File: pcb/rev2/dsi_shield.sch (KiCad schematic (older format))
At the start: 18 parts, among them CN10 CVBS In, CN5 IOH, CN6 POWER_UNO, CN7 IOL, CN8 AD, IC12 OSC_25MHZ_PERICOM_FNETHE025

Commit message: pcb wip
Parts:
- B1, B2, B3, B4: footprint c350h200 -> Pads:c350h200
- C17: footprint CAPC1608X90N -> Capacitors SMD:CAPC1608X90N
- D9: footprint SOD3715X145N -> ICs And Semiconductors SMD:SOD3715X145N
- FTG1, FTG2, FTG3, FTG4, FTG5, FTG6: footprint FIDUCIAL_TOP_S100-200 -> Pads:FIDUCIAL_TOP_S100-200
- IC12: footprint OSC_PERICOM_FNETHE025 -> ICs And Semiconductors SMD:OSC_PERICOM_FNETHE025
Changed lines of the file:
@@
 F 0 "IC12" H 6150 7415 50  0000 C CNN
 F 1 "OSC_25MHZ_PERICOM_FNETHE025" H 5850 6660 60  0001 L CNN
-F 2 "OSC_PERICOM_FNETHE025" H 5850 5760 60  0001 L CNN
+F 2 "ICs And Semiconductors SMD:OSC_PERICOM_FNETHE025" H 5850 5760 60  0001 L CNN
 F 3 "\\cern.ch\\dfs\\Applications\\Altium\\Datasheets\\OSC_PERICOM_FNETHE025.pdf" H 5850 6480 60  0001 L CNN
 F 4 "25MHz" H 6150 7324 50  0000 C CNN "~"
@@
 F 0 "C17" V 5754 7860 50  0000 L CNN
 F 1 "CC0603_100NF_100V_10%_X7R" H 5650 7490 60  0001 L CNN
-F 2 "CAPC1608X90N" H 5650 6680 60  0001 L CNN
+F 2 "Capacitors SMD:CAPC1608X90N" H 5650 6680 60  0001 L CNN
 F 3 "\\cern.ch\\dfs\\Applications\\Altium\\Datasheets\\CC0603_MURATA_GRM188R72A104KA35D.pdf" H 5650 7310 60  0001 L CNN
 F 4 "100nF" V 5845 7860 50  0000 L CNN "~"
@@
 F 0 "B1" H 6600 9950 50  0000 C CNN
 F 1 "PLATED_HOLE2.0_PAD3.5" H 6500 9780 60  0001 L CNN
-F 2 "c350h200" H 6500 8970 60  0001 L CNN
+F 2 "Pads:c350h200" H 6500 8970 60  0001 L CNN
 F 3 "Undefined" H 6500 9600 60  0001 L CNN
 F 4 "Plated Hole" H 6500 9510 60  0001 L CNN "Field4"
@@
 F 0 "B2" H 6600 10050 50  0000 C CNN
 F 1 "PLATED_HOLE2.0_PAD3.5" H 6500 9880 60  0001 L CNN
-F 2 "c350h200" H 6500 9070 60  0001 L CNN
+F 2 "Pads:c350h200" H 6500 9070 60  0001 L CNN
 F 3 "Undefined" H 6500 9700 60  0001 L CNN
 F 4 "Plated Hole" H 6500 9610 60  0001 L CNN "Field4"
@@
 F 0 "B3" H 6600 10150 50  0000 C CNN
 F 1 "PLATED_HOLE2.0_PAD3.5" H 6500 9980 60  0001 L CNN
-F 2 "c350h200" H 6500 9170 60  0001 L CNN
+F 2 "Pads:c350h200" H 6500 9170 60  0001 L CNN
 F 3 "Undefined" H 6500 9800 60  0001 L CNN
 F 4 "Plated Hole" H 6500 9710 60  0001 L CNN "Field4"
@@
 F 0 "B4" H 6600 10250 50  0000 C CNN
 F 1 "PLATED_HOLE2.0_PAD3.5" H 6500 10080 60  0001 L CNN
-F 2 "c350h200" H 6500 9270 60  0001 L CNN
+F 2 "Pads:c350h200" H 6500 9270 60  0001 L CNN
 F 3 "Undefined" H 6500 9900 60  0001 L CNN
 F 4 "Plated Hole" H 6500 9810 60  0001 L CNN "Field4"
@@
 F 0 "FTG1" H 7038 10050 50  0000 L CNN
 F 1 "FIDUCIAL_TARGET_S100-200" H 6950 9900 60  0001 L CNN
-F 2 "FIDUCIAL_TOP_S100-200" H 6950 9090 60  0001 L CNN
+F 2 "Pads:FIDUCIAL_TOP_S100-200" H 6950 9090 60  0001 L CNN
 F 3 "Undefined" H 6950 9720 60  0001 L CNN
 F 4 "~~" H 6950 9630 60  0001 L CNN "Field4"
@@
 F 0 "FTG2" H 7438 10050 50  0000 L CNN
 F 1 "FIDUCIAL_TARGET_S100-200" H 7350 9900 60  0001 L CNN
-F 2 "FIDUCIAL_TOP_S100-200" H 7350 9090 60  0001 L CNN
+F 2 "Pads:FIDUCIAL_TOP_S100-200" H 7350 9090 60  0001 L CNN
 F 3 "Undefined" H 7350 9720 60  0001 L CNN
 F 4 "~~" H 7350 9630 60  0001 L CNN "Field4"
@@
 F 0 "FTG6" H 7438 10350 50  0000 L CNN
 F 1 "FIDUCIAL_TARGET_S100-200" H 7350 10200 60  0001 L CNN
-F 2 "FIDUCIAL_TOP_S100-200" H 7350 9390 60  0001 L CNN
+F 2 "Pads:FIDUCIAL_TOP_S100-200" H 7350 9390 60  0001 L CNN
 F 3 "Undefined" H 7350 10020 60  0001 L CNN
 F 4 "~~" H 7350 9930 60  0001 L CNN "Field4"
@@
 F 0 "FTG5" H 7038 10350 50  0000 L CNN
 F 1 "FIDUCIAL_TARGET_S100-200" H 6950 10200 60  0001 L CNN
-F 2 "FIDUCIAL_TOP_S100-200" H 6950 9390 60  0001 L CNN
+F 2 "Pads:FIDUCIAL_TOP_S100-200" H 6950 9390 60  0001 L CNN
 F 3 "Undefined" H 6950 10020 60  0001 L CNN
 F 4 "~~" H 6950 9930 60  0001 L CNN "Field4"
@@
 F 0 "FTG4" H 7838 10350 50  0000 L CNN
 F 1 "FIDUCIAL_TARGET_S100-200" H 7750 10200 60  0001 L CNN
-F 2 "FIDUCIAL_TOP_S100-200" H 7750 9390 60  0001 L CNN
+F 2 "Pads:FIDUCIAL_TOP_S100-200" H 7750 9390 60  0001 L CNN
 F 3 "Undefined" H 7750 10020 60  0001 L CNN
 F 4 "~~" H 7750 9930 60  0001 L CNN "Field4"
@@
 F 0 "FTG3" H 7838 10050 50  0000 L CNN
 F 1 "FIDUCIAL_TARGET_S100-200" H 7750 9900 60  0001 L CNN
-F 2 "FIDUCIAL_TOP_S100-200" H 7750 9090 60  0001 L CNN
+F 2 "Pads:FIDUCIAL_TOP_S100-200" H 7750 9090 60  0001 L CNN
 F 3 "Undefined" H 7750 9720 60  0001 L CNN
 F 4 "~~" H 7750 9630 60  0001 L CNN "Field4"
@@
 F 0 "D9" V 1496 4060 50  0000 R CNN
 F 1 "MBR0530PbF" V 1405 4060 50  0000 R CNN
-F 2 "SOD3715X145N" H 1300 3010 60  0001 L CNN
+F 2 "ICs And Semiconductors SMD:SOD3715X145N" H 1300 3010 60  0001 L CNN
 F 3 "\\cern.ch\\dfs\\Applications\\Altium\\Datasheets\\MBR0530PBF.pdf" H 1300 3730 60  0001 L CNN
 F 4 "MBR0530PbF" H 1300 3640 60  0001 L CNN "Part Number"

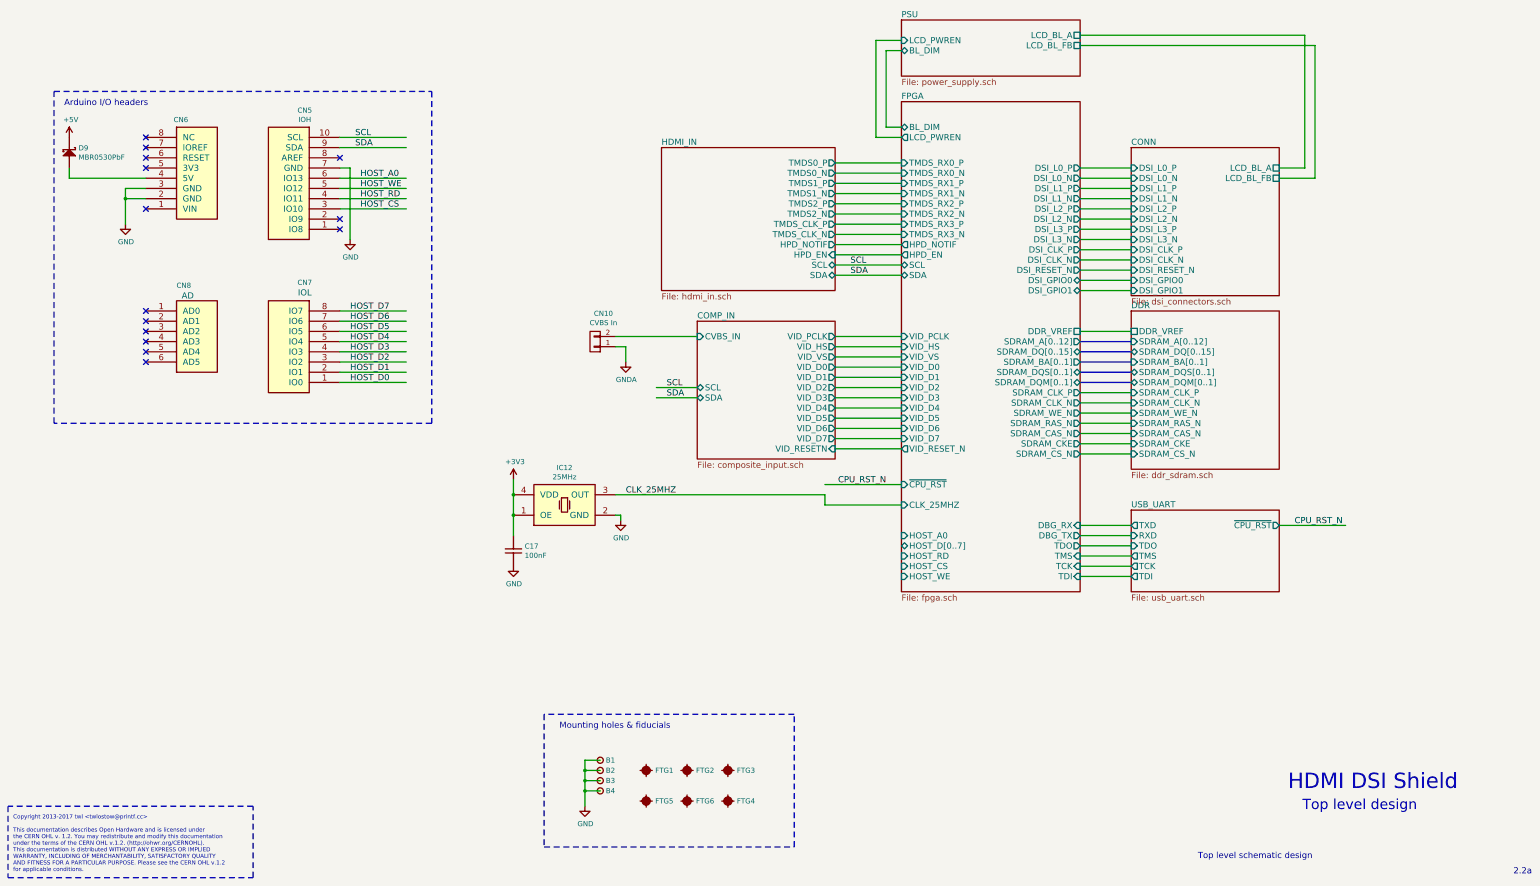
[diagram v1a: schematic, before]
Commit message: Completed port to KiCad, passes DRC+LVS. NOT MANUFACTURED.
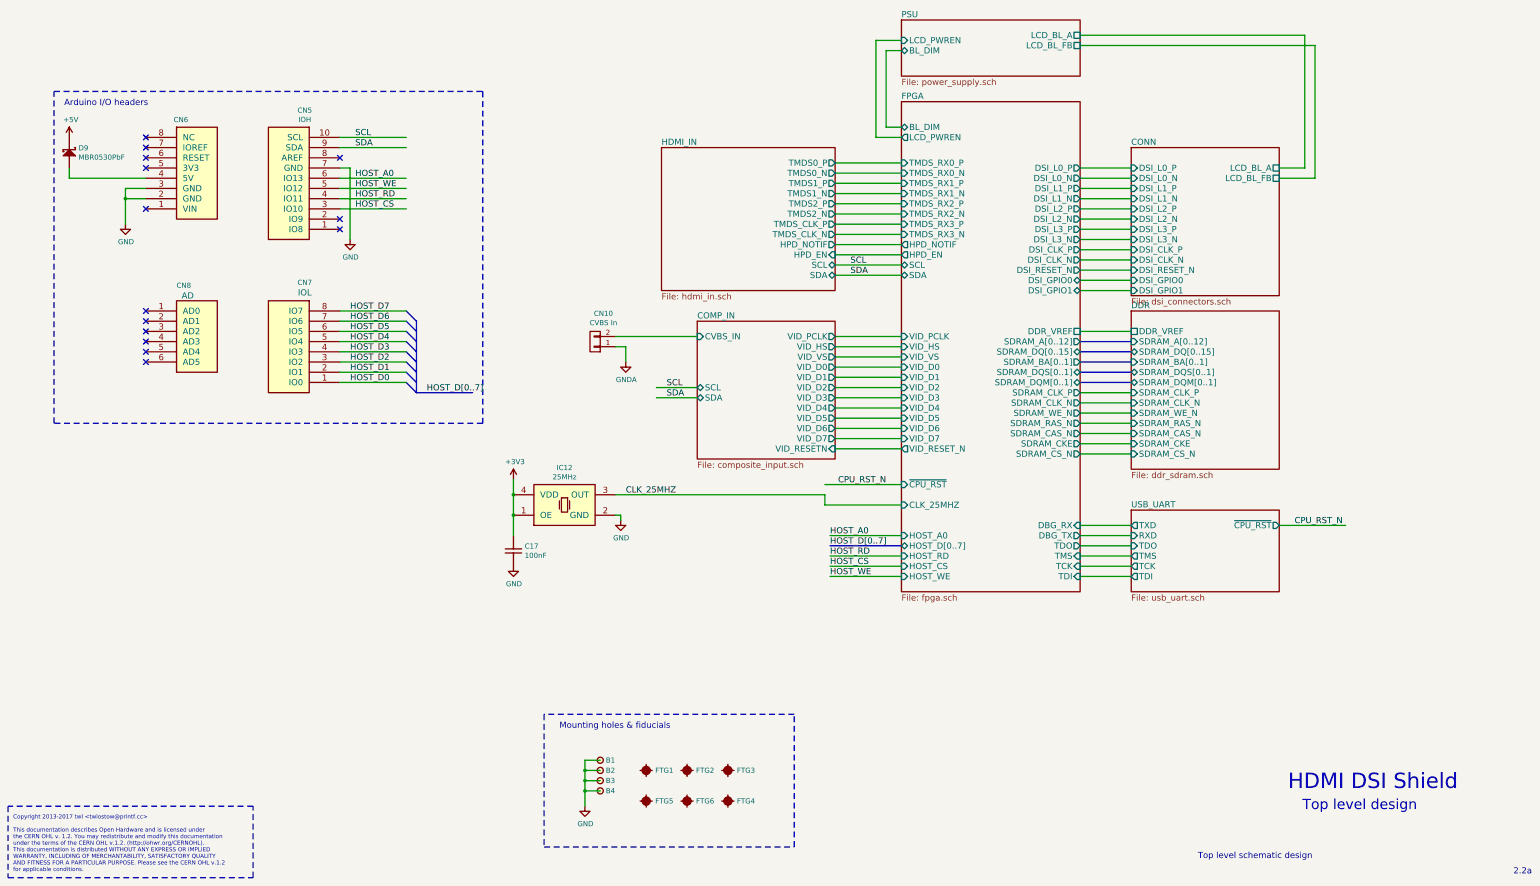
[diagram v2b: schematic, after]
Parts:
- CN10: footprint (none) -> Pin_Headers:Pin_Header_Straight_1x02; Fieldname (none) -> Value
- CN5: footprint (none) -> Pin_Headers:Pin_Header_Straight_1x10; Fieldname (none) -> Value
- CN6: footprint (none) -> Pin_Headers:Pin_Header_Straight_1x08; Fieldname (none) -> Value
- CN7: footprint (none) -> Pin_Headers:Pin_Header_Straight_1x08
- CN8: footprint (none) -> Pin_Headers:Pin_Header_Straight_1x06
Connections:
- net labels added: HOST_D[0..7]
- wire segments 102 -> 106

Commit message: axi4/zynq version: wip
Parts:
- B1, B2, B3, B4: symbol PLATED_HOLE2.0_PAD3.5 -> dsi_shield-rescue:PLATED_HOLE2.0_PAD3.5-
- C17: symbol CC0603_100NF_100V_10%_X7R -> dsi_shield-rescue:CC0603_100NF_100V_10%_X7R-
- CN10: symbol CONN_01X02 -> dsi_shield-rescue:CONN_01X02-
- CN5: symbol IOH -> dsi_shield-rescue:IOH-
- CN6: symbol POWER_UNO -> dsi_shield-rescue:POWER_UNO-
- CN7: symbol IOL -> dsi_shield-rescue:IOL-
- CN8: symbol AD -> dsi_shield-rescue:AD-
- D9: symbol MBR0530PbF -> dsi_shield-rescue:MBR0530PbF-
- FTG1, FTG2, FTG3, FTG4, FTG5, FTG6: symbol FIDUCIAL_TARGET_S100-200 -> dsi_shield-rescue:FIDUCIAL_TARGET_S100-200-
- IC12: symbol OSC_25MHZ_PERICOM_FNETHE025 -> dsi_shield-rescue:OSC_25MHZ_PERICOM_FNETHE025-
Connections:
- wire segments 106 -> 112
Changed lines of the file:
@@
-EESchema Schematic File Version 2
-LIBS:Capacitors Networks THD
-LIBS:Capacitors Networks SMD
-LIBS:Capacitors THD
-LIBS:Capacitors SMD
-LIBS:Miscellaneous
-LIBS:HARWIN
-LIBS:LEMO
-LIBS:WEIDMULLER
-LIBS:FCI
-LIBS:MOLEX
-LIBS:TYCO
-LIBS:ERNI
-LIBS:MENTOR
-LIBS:SAMTEC
-LIBS:STELVIO-KONTEK COMATEL
-LIBS:AMPHENOL
-LIBS:HARTING
-LIBS:3M
-LIBS:Pads
-LIBS:Switches
-LIBS:Relays
-LIBS:Heat-Sinks
-LIBS:Fasteners & Fixings
-LIBS:Batteries
-LIBS:Fuses
-LIBS:Metal Screening Box
-LIBS:Sockets
-LIBS:Regulators
-LIBS:Transistors
-LIBS:Power Supplies
-LIBS:Analog & Interface
-LIBS:Sensors
-LIBS:Logic
-LIBS:Optocouplers
-LIBS:Standard Logic
-LIBS:DC-DC Converters
-LIBS:Operational Amplifiers
-LIBS:Crystals & Oscillators
-LIBS:Diodes
-LIBS:LEDs & Displays
-LIBS:PCB Modules
-LIBS:Bonding
-LIBS:Resistors THD
-LIBS:Potentiometers SMD
-LIBS:Thermistors And Varistors
-LIBS:Potentiometers THD
-LIBS:Resistor Networks THD
-LIBS:Resistors SMD
-LIBS:Resistor Networks SMD
-LIBS:Transformers
-LIBS:Inductors SMD
-LIBS:Inductors THD
-LIBS:Cores
-LIBS:power
-LIBS:conn
-LIBS:dsi_shield
+EESchema Schematic File Version 4
 LIBS:dsi_shield-cache
 EELAYER 26 0
@@
 $EndSheet
 $Comp
-L OSC_25MHZ_PERICOM_FNETHE025 IC12
+L dsi_shield-rescue:OSC_25MHZ_PERICOM_FNETHE025- IC12
 U 1 1 5992C2E4
 P 5850 7250
@@
 $EndComp
 $Comp
-L +3V3 #PWR01
+L dsi_shield-rescue:+3V3- #PWR01
 U 1 1 5992D2A2
 P 5650 7200
@@
 $EndComp
 $Comp
-L CC0603_100NF_100V_10%_X7R C17
+L dsi_shield-rescue:CC0603_100NF_100V_10%_X7R- C17
 U 1 1 5992E213
 P 5650 7750
@@
 $EndComp
 $Comp
-L GND #PWR02
+L dsi_shield-rescue:GND- #PWR02
 U 1 1 5992E674
 P 5650 8050
@@
 $EndComp
 $Comp
-L GND #PWR03
+L dsi_shield-rescue:GND- #PWR03
 U 1 1 5992E91D
 P 6700 7600
@@
 CLK_25MHZ
 $Comp
-L PLATED_HOLE2.0_PAD3.5 B1
+L dsi_shield-rescue:PLATED_HOLE2.0_PAD3.5- B1
 U 1 1 59932F22
 P 6500 9950
@@
 $EndComp
 $Comp
-L PLATED_HOLE2.0_PAD3.5 B2
+L dsi_shield-rescue:PLATED_HOLE2.0_PAD3.5- B2
 U 1 1 599342E5
 P 6500 10050
@@
 $EndComp
 $Comp
-L PLATED_HOLE2.0_PAD3.5 B3
+L dsi_shield-rescue:PLATED_HOLE2.0_PAD3.5- B3
 U 1 1 599344FA
 P 6500 10150
@@
 $EndComp
 $Comp
-L PLATED_HOLE2.0_PAD3.5 B4
+L dsi_shield-rescue:PLATED_HOLE2.0_PAD3.5- B4
 U 1 1 59934715
 P 6500 10250
@@
 $EndComp
 $Comp
-L GND #PWR04
+L dsi_shield-rescue:GND- #PWR04
 U 1 1 59934D89
 P 6350 10400
@@
 CPU_RST_N
 $Comp
-L FIDUCIAL_TARGET_S100-200 FTG1
+L dsi_shield-rescue:FIDUCIAL_TARGET_S100-200- FTG1
 U 1 1 599436EB
 P 6950 10050
@@
 $EndComp
 $Comp
-L FIDUCIAL_TARGET_S100-200 FTG2
+L dsi_shield-rescue:FIDUCIAL_TARGET_S100-200- FTG2
 U 1 1 599440AC
 P 7350 10050
@@
 $EndComp
 $Comp
-L FIDUCIAL_TARGET_S100-200 FTG6
+L dsi_shield-rescue:FIDUCIAL_TARGET_S100-200- FTG6
 U 1 1 599443FB
 P 7350 10350
@@
 $EndComp
 $Comp
-L FIDUCIAL_TARGET_S100-200 FTG5
+L dsi_shield-rescue:FIDUCIAL_TARGET_S100-200- FTG5
 U 1 1 59944748
 P 6950 10350
@@
 $EndComp
 $Comp
-L FIDUCIAL_TARGET_S100-200 FTG4
+L dsi_shield-rescue:FIDUCIAL_TARGET_S100-200- FTG4
 U 1 1 59944A9B
 P 7750 10350
@@
 $EndComp
 $Comp
-L FIDUCIAL_TARGET_S100-200 FTG3
+L dsi_shield-rescue:FIDUCIAL_TARGET_S100-200- FTG3
 U 1 1 59944DEC
 P 7750 10050
@@
 SDA
 $Comp
-L IOH CN5
+L dsi_shield-rescue:IOH- CN5
 U 1 1 5994E05C
 P 3650 4750
@@
 $EndComp
 $Comp
-L IOL CN7
+L dsi_shield-rescue:IOL- CN7
 U 1 1 5994E87B
 P 3650 6250
@@
 $EndComp
 $Comp
-L POWER_UNO CN6
+L dsi_shield-rescue:POWER_UNO- CN6
 U 1 1 5994EDEB
-P 2350 4550
-F 0 "CN6" H 2393 3677 50  0000 C CNN
-F 1 "POWER_UNO" H 2350 3560 60  0001 L CNN
-F 2 "Pin_Headers:Pin_Header_Straight_1x08" H 2350 3470 60  0001 L CNN
-F 3 "" H 2350 3380 60  0001 L CNN
-F 4 "Value" H 2350 4550 60  0001 C CNN "Fieldname"
-F 5 "Yes" H 2350 3290 60  0001 L CNN "Field4"
-F 6 "POWER" H 2350 3200 60  0001 L CNN "Field5"
-	1    2350 4550
-	1    0    0    1
-$EndComp
-$Comp
-L CONN_01X02 CN10
+P 2350 3850
+F 0 "CN6" H 2393 2977 50  0000 C CNN
+F 1 "POWER_UNO" H 2350 2860 60  0001 L CNN
+F 2 "Pin_Headers:Pin_Header_Straight_1x08" H 2350 2770 60  0001 L CNN
+F 3 "" H 2350 2680 60  0001 L CNN
+F 4 "Value" H 2350 3850 60  0001 C CNN "Fieldname"
+F 5 "Yes" H 2350 2590 60  0001 L CNN "Field4"
+F 6 "POWER" H 2350 2500 60  0001 L CNN "Field5"
+	1    2350 3850
+	1    0    0    -1
+$EndComp
+$Comp
+L dsi_shield-rescue:CONN_01X02- CN10
 U 1 1 5994F8EB
 P 6450 5850
@@
 $EndComp
 $Comp
-L GNDA #PWR05
+L dsi_shield-rescue:GNDA- #PWR05
 U 1 1 5995A62E
 P 6750 6050
@@
 $EndComp
 $Comp
-L MBR0530PbF D9
+L dsi_shield-rescue:MBR0530PbF- D9
 U 1 1 5995E5F7
 P 1300 4150
@@
 $EndComp
 $Comp
-L +5V #PWR06
+L dsi_shield-rescue:+5V- #PWR06
 U 1 1 59963732
 P 1300 3850
@@
 $EndComp
 $Comp
-L GND #PWR07
+L dsi_shield-rescue:GND- #PWR07
 U 1 1 5996428F
 P 1850 4700
@@
 SDA
 $Comp
-L GND #PWR08
+L dsi_shield-rescue:GND- #PWR08
 U 1 1 599708A5
 P 4050 4850
@@
 HOST_D0
 $Comp
-L AD CN8
+L dsi_shield-rescue:AD- CN8
 U 1 1 5997B8AD
 P 2350 5550
@@
 	3100 10400 700  10400
 Wire Wire Line
-	5650 7200 5650 7750
+	5650 7200 5650 7350
 Connection ~ 5650 7550
 Connection ~ 5650 7350
@@
 	6500 9950 6350 9950
 Wire Wire Line
-	6350 9950 6350 10400
+	6350 9950 6350 10050
 Wire Wire Line
 	6500 10250 6350 10250
@@
 	2050 4350 1850 4350
 Wire Wire Line
-	1850 4350 1850 4700
+	1850 4350 1850 4450
 Wire Wire Line
 	2050 4450 1850 4450
@@
 	1150 6650 1150 3400
 Wire Bus Line
-	4700 5650 4700 6350
-Wire Bus Line
 	4700 6350 5250 6350
 Wire Wire Line
@@
 Wire Bus Line
 	9450 7850 8750 7850
+Wire Wire Line
+	5650 7550 5650 7750
+Wire Wire Line
+	5650 7350 5650 7550
+Wire Wire Line
+	6350 10250 6350 10400
+Wire Wire Line
+	6350 10150 6350 10250
+Wire Wire Line
+	6350 10050 6350 10150
+Wire Wire Line
+	1850 4450 1850 4700
+Wire Bus Line
+	4700 5650 4700 6350
 $EndSCHEMATC
